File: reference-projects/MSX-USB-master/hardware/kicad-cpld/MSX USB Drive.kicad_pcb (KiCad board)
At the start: 2 copper layers, 88.9 x 63.6 mm, 9 parts, among them J1 AVR-JTAG-10, J2 Conn_02x08_Odd_Even, U1 EPM7032_7064, U5 AM29f040-lrj

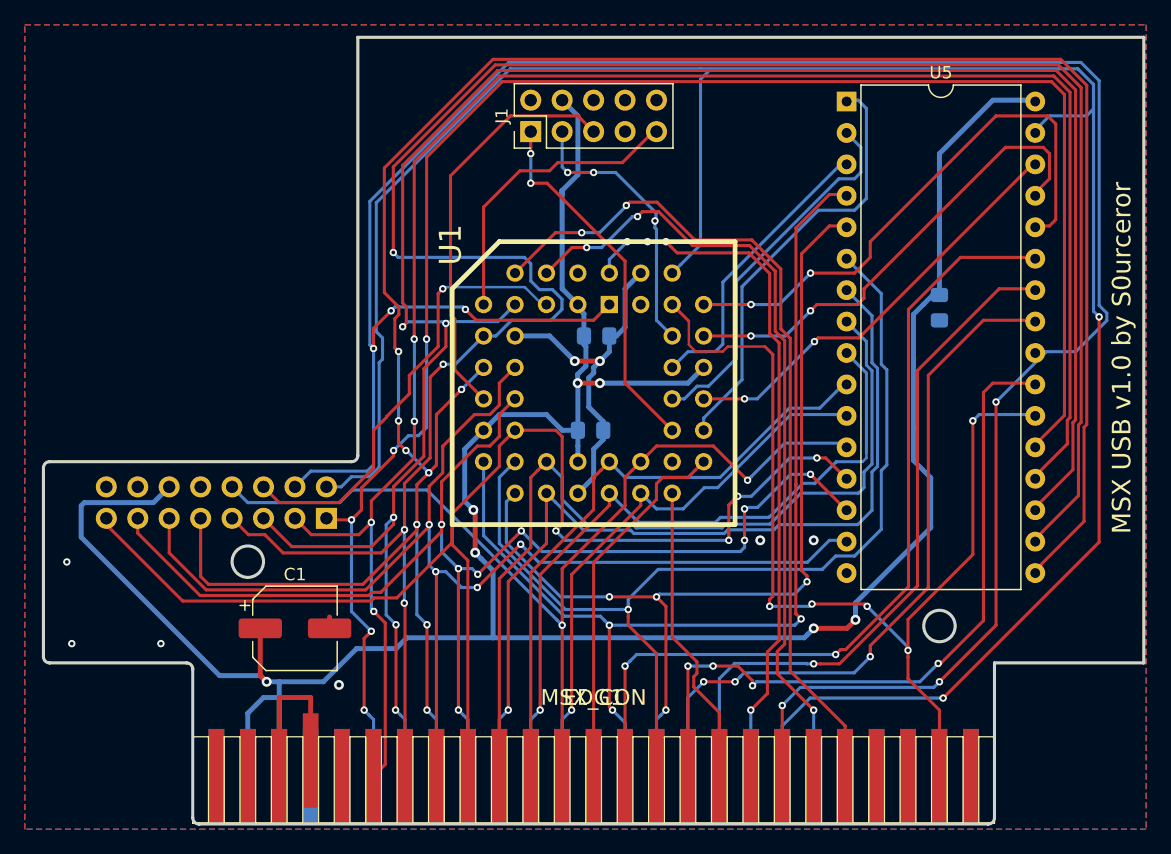
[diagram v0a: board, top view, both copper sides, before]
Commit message: Added cooler and CPU-mount footprints, as well as Indication LEDs.
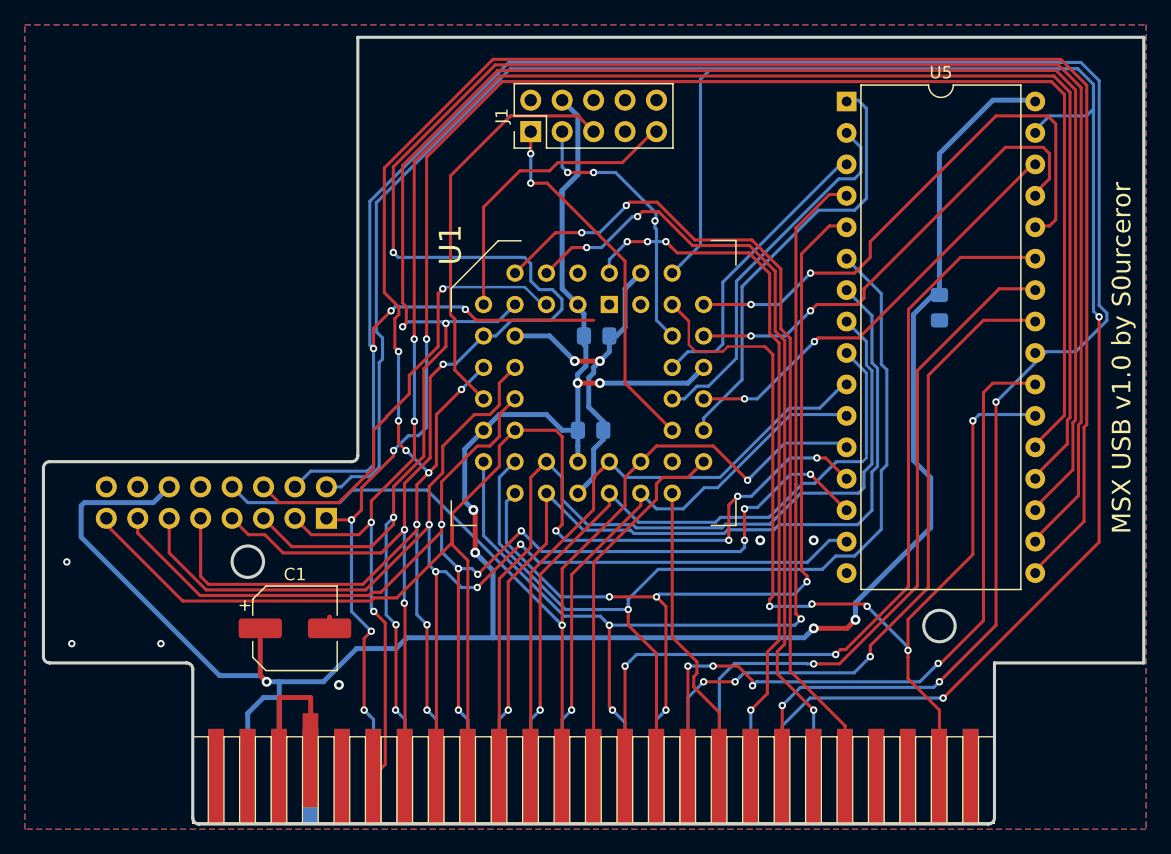
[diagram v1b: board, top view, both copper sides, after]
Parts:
- moved EDG1 37.3 mm to (644.4, -666.2)
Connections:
- EDG1 pad +12V: Net-(EDG1-Pad+12V) -> unconnected-(EDG1-Pad+12V)
- EDG1 pad -12V: Net-(EDG1-Pad-12V) -> unconnected-(EDG1-Pad-12V)
- EDG1 pad /CS1: Net-(EDG1-Pad/CS1) -> unconnected-(EDG1-Pad/CS1)
- EDG1 pad /CS12: Net-(EDG1-Pad/CS12) -> unconnected-(EDG1-Pad/CS12)
- EDG1 pad /CS2: Net-(EDG1-Pad/CS2) -> unconnected-(EDG1-Pad/CS2)
- EDG1 pad /INT: Net-(EDG1-Pad/INT) -> unconnected-(EDG1-Pad/INT)
- EDG1 pad /M1: Net-(EDG1-Pad/M1) -> unconnected-(EDG1-Pad/M1)
- EDG1 pad /MREQ: Net-(EDG1-Pad/MREQ) -> unconnected-(EDG1-Pad/MREQ)
- EDG1 pad /RESV1: Net-(EDG1-Pad/RESV1) -> unconnected-(EDG1-Pad/RESV1)
- EDG1 pad /RESV2: Net-(EDG1-Pad/RESV2) -> unconnected-(EDG1-Pad/RESV2)
- EDG1 pad /RFSH: Net-(EDG1-Pad/RFSH) -> unconnected-(EDG1-Pad/RFSH)
- EDG1 pad /WAIT: Net-(EDG1-Pad/WAIT) -> unconnected-(EDG1-Pad/WAIT)
- EDG1 pad A14: Net-(EDG1-PadA14) -> unconnected-(EDG1-PadA14)
- EDG1 pad CLOCK: Net-(EDG1-PadCLOCK) -> unconnected-(EDG1-PadCLOCK)
- EDG1 pad SOUNDIN: Net-(EDG1-PadSOUNDIN) -> unconnected-(EDG1-PadSOUNDIN)
- J1 pad 6: Net-(J1-Pad6) -> unconnected-(J1-Pad6)
- J1 pad 7: Net-(J1-Pad7) -> unconnected-(J1-Pad7)
- J1 pad 8: Net-(J1-Pad8) -> unconnected-(J1-Pad8)
- J2 pad 10: Net-(J2-Pad10) -> unconnected-(J2-Pad10)
- U1 pad 1: /RD_ -> unconnected-(U1-Pad1)
- U1 pad 2: Net-(U1-Pad2) -> unconnected-(U1-Pad2)
- U1 pad 43: Net-(U1-Pad43) -> /RD_
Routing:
- net /TDO: track 22.5 -> 0.00 mm, vias 3 -> 0
- net /RESET_: track 57.6 -> 80.1 mm, vias 4 -> 7
- net /RD_: track 190.1 -> 188.3 mm
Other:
- net class Default removed
- net class Power removed
